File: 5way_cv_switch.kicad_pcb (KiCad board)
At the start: 2 copper layers, 29 x 22 mm, 18 parts, among them J1 I/O connector, J2 5-way Switch Connector, U1 HT7550-1, U2 opamp_dbv2

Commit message: minor updates
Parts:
- removed REF**: hole_2.65mm, cycfi_library:hole_2.65mm
- added H5: MountingHole, cycfi_library:hole_2.65mm, F.Cu at (149.7, 49.8)
- moved G*** 0.14 mm to (145.7, 40.1)

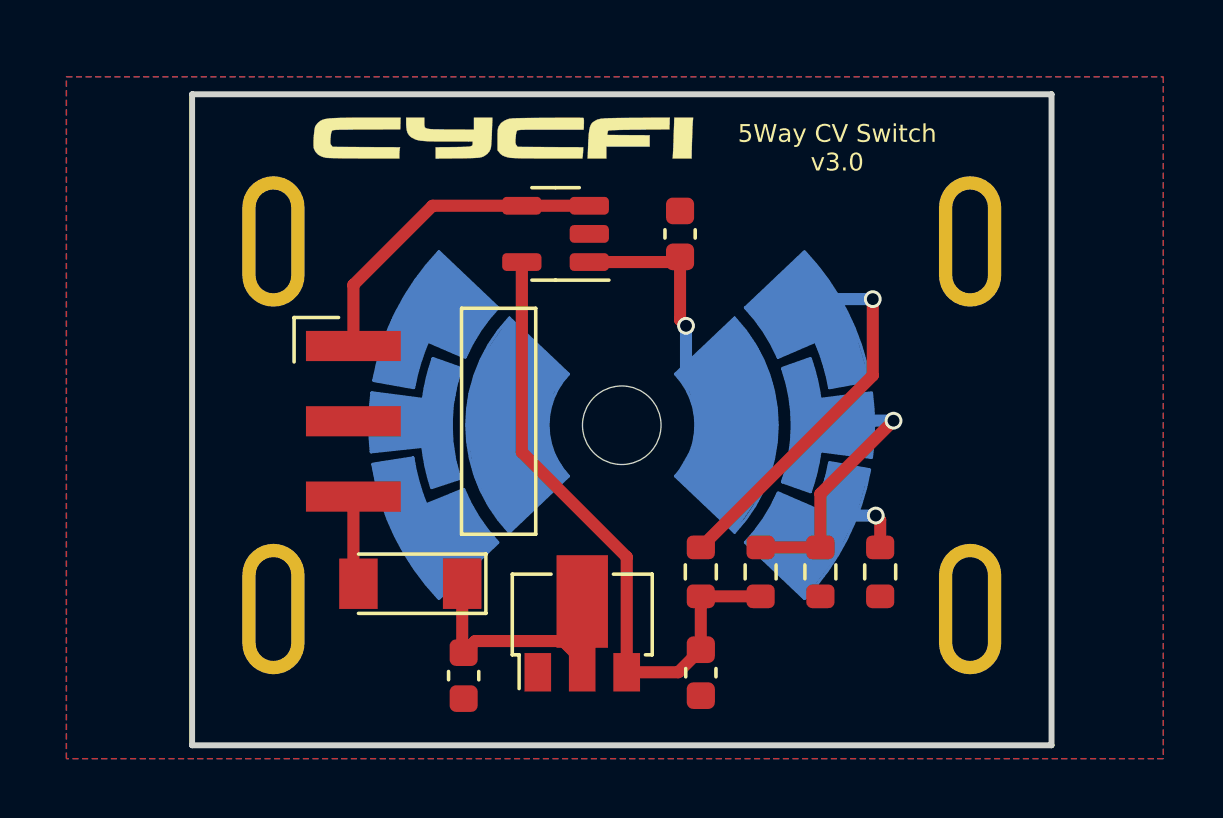
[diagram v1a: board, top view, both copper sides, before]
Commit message: Updated components for JLCPCB PCBA
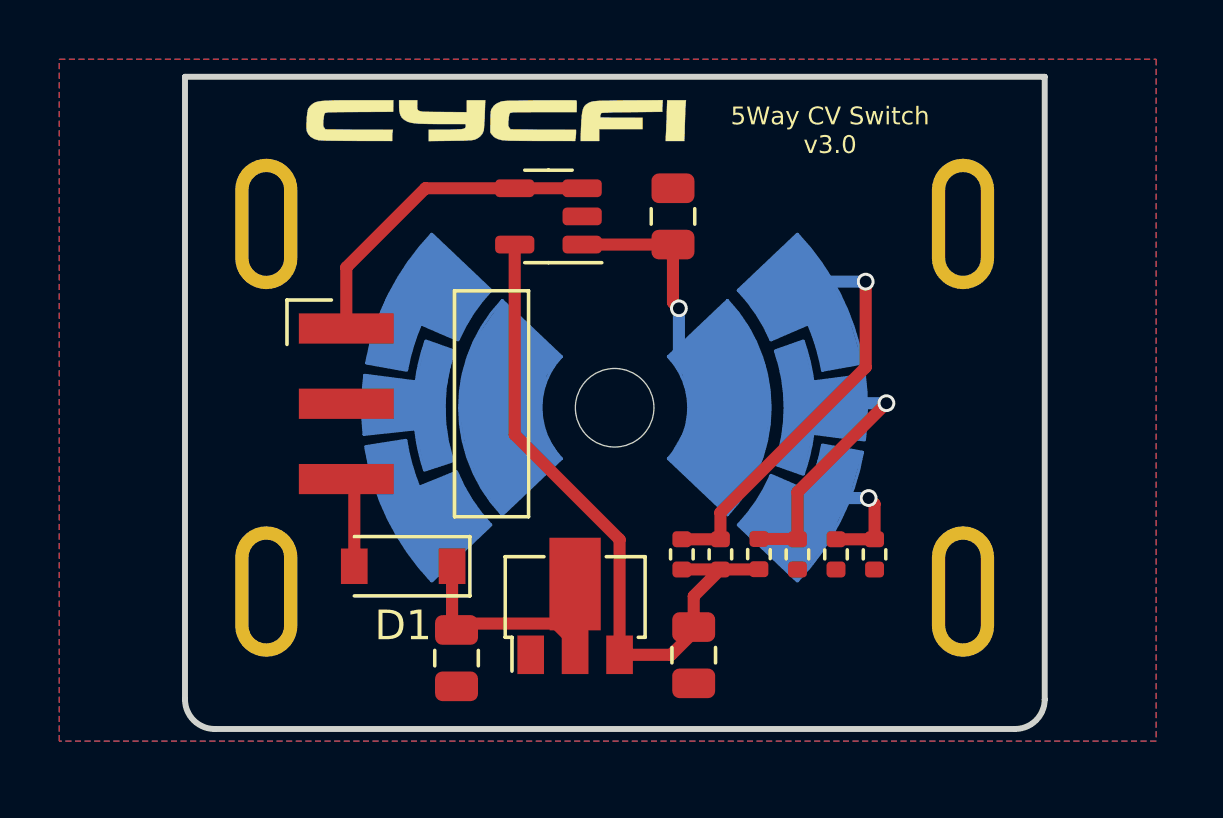
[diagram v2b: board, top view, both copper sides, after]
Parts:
- added R5: 47k, Resistor_SMD:R_0402_1005Metric, F.Cu at (153.1, 54.1)
- added R6: 47k, Resistor_SMD:R_0402_1005Metric, F.Cu at (157.0, 54.1)
- C1, C2, C3: footprint Capacitor_SMD:C_0603_1608Metric -> Capacitor_SMD:C_0805_2012Metric
- D1: value LL4148 -> 1N4148W; footprint Diode_SMD:D_MiniMELF -> Diode_SMD:D_SOD-123
- R1, R2: value 30k -> 47k; footprint Resistor_SMD:R_0603_1608Metric -> Resistor_SMD:R_0402_1005Metric
- R3, R4: value 15k -> 47k; footprint Resistor_SMD:R_0603_1608Metric -> Resistor_SMD:R_0402_1005Metric
- U2: value opamp_dbv2 -> LMV321IDBVR
- moved R2 0.97 mm to (155.7, 54.1)
- moved R3 0.87 mm to (151.8, 54.1)
- moved C1 0.64 mm to (144.2, 57.6)
- moved C2 0.64 mm to (152.2, 57.5)
- moved H1 0.64 mm to (137.7, 55.4)
- moved H2 0.64 mm to (161.2, 55.4)
- moved H3 0.64 mm to (137.7, 43.0)
- moved H4 0.64 mm to (161.2, 43.0)
- moved U1 0.64 mm to (148.2, 55.8)
- moved H5 0.64 mm to (149.5, 49.2)
- moved J1 0.64 mm to (140.4, 46.5)
- moved U2 0.64 mm to (147.3, 42.7)
- moved D1 0.64 mm to (142.4, 54.5)
- moved G*** 0.64 mm to (145.5, 39.5)
- moved J2 0.64 mm to (149.5, 49.2)
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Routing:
- net bridge: track 3.92 -> 5.55 mm
- net neck: track 13.4 -> 14.7 mm
- net 5v: track 21.9 -> 23.0 mm
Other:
- outline, holes or cut-outs redrawn
